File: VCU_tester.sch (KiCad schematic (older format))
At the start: 40 parts, among them J1 Conn_01x04_Male, J12 Conn_01x08_Male, J13 Conn_01x08_Male, J14 USB_C_Receptacle, J15 USB_B_Micro, J2 Screw_Terminal_01x02, J500 Conn_01x08_Female, J501 Conn_01x08_Female, J502 Conn_01x08_Female, J504 Conn_02x18_Odd_Even, J505 Conn_01x10_Female, J506 Conn_01x08_Female, J507 Conn_01x08_Female, J7 Conn_01x04_Male, P8 BeagleBone_Black_Header, P9 BeagleBone_Black_Header, U1 REF3020, U6 DS3231MZ, U7 DS3231MZ

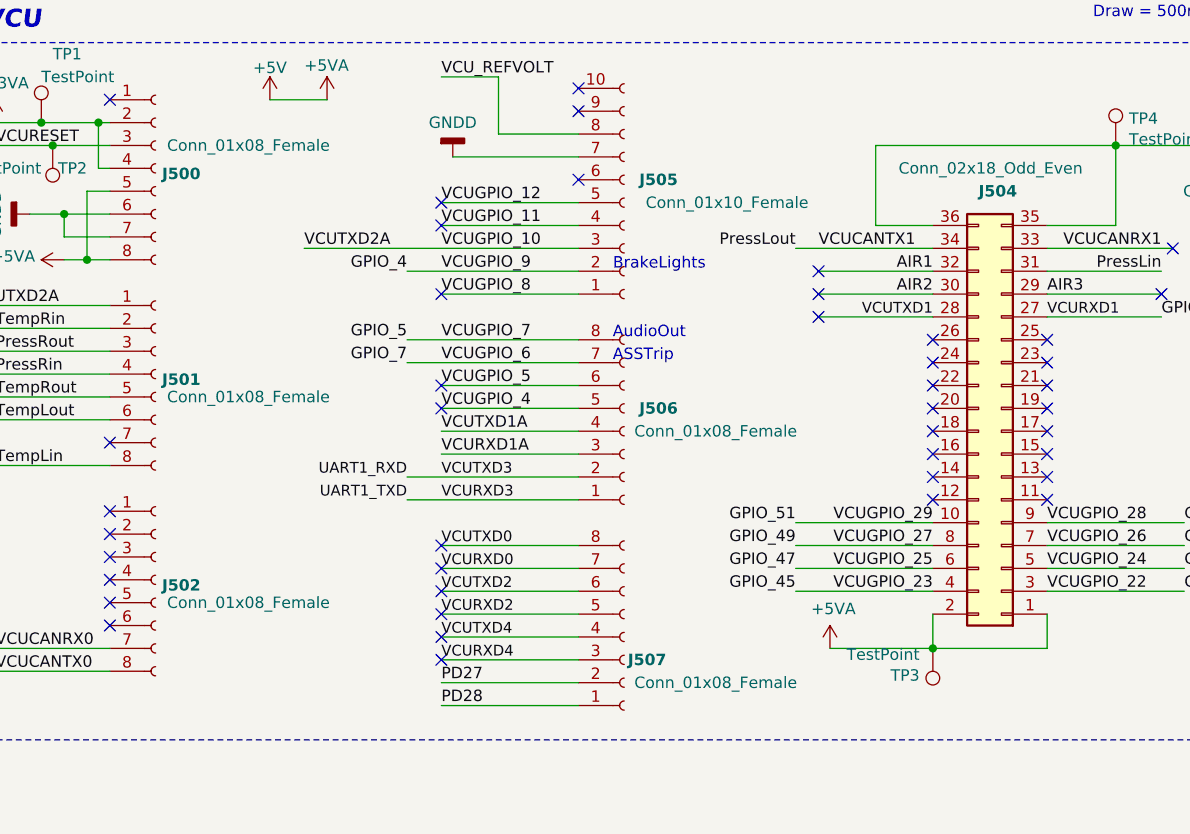
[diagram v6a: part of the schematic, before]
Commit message: placed vcu and beaglebone
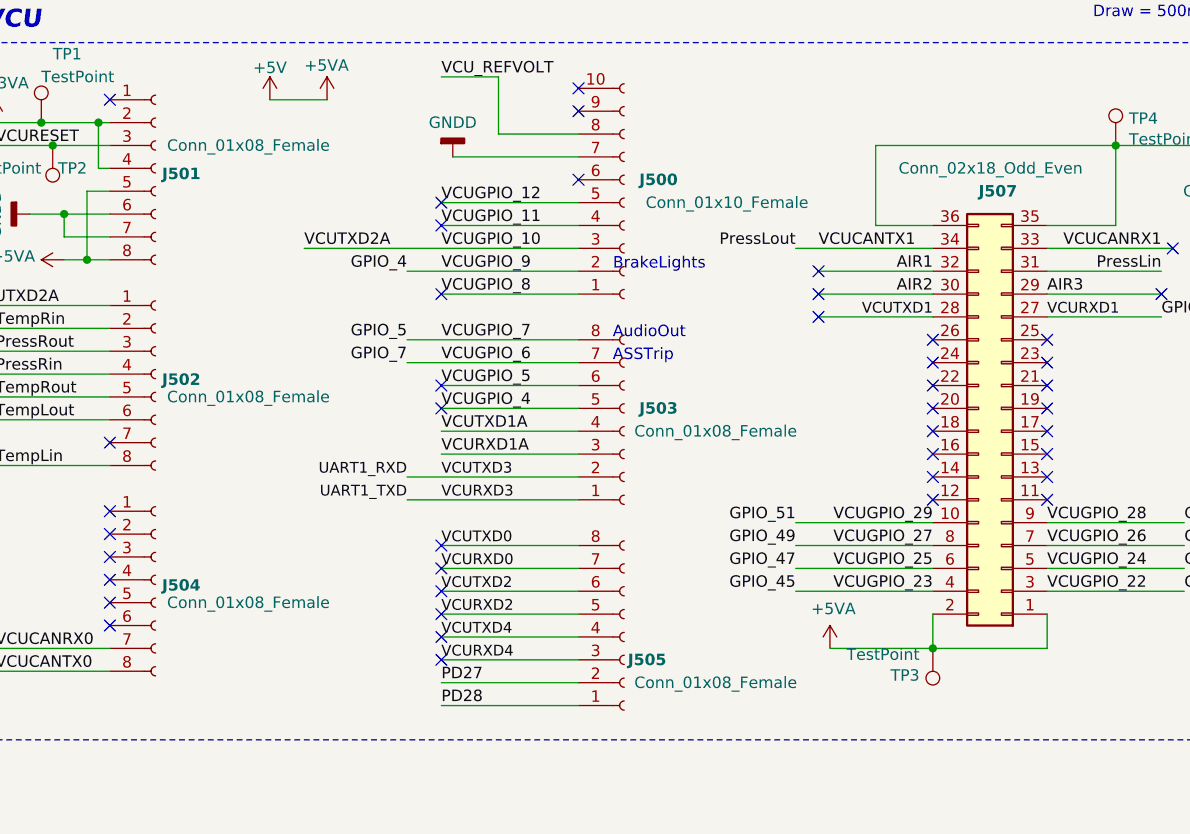
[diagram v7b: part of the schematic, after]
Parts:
- P8, P9: footprint Socket_BeagleBone_Black:Socket_BeagleBone_Black -> project:PinHeader_2x23_P2.54mm_Vertical_Flip
- renumbered J505 to J500, J500 to J501, J501 to J502, J506 to J503, J502 to J504, J507 to J505, J504 to J507
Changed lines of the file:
@@
 F 0 "P9" H 2400 3650 50  0000 C CNN
 F 1 "BeagleBone_Black_Header" V 2450 2500 50  0000 C CNN
-F 2 "Socket_BeagleBone_Black:Socket_BeagleBone_Black" H 2400 1600 60  0001 C CNN
+F 2 "project:PinHeader_2x23_P2.54mm_Vertical_Flip" H 2400 1600 60  0001 C CNN
 F 3 "" H 2400 1600 60  0000 C CNN
 F 4 "1528-1365-ND" H 2400 2450 50  0001 C CNN "Part"
@@
 F 0 "P8" H 4700 3650 50  0000 C CNN
 F 1 "BeagleBone_Black_Header" V 4750 2500 50  0000 C CNN
-F 2 "Socket_BeagleBone_Black:Socket_BeagleBone_Black" H 4700 1600 60  0001 C CNN
+F 2 "project:PinHeader_2x23_P2.54mm_Vertical_Flip" H 4700 1600 60  0001 C CNN
 F 3 "" H 4700 1600 60  0000 C CNN
 F 4 "1528-1365-ND" H 4700 2450 50  0001 C CNN "Part"
@@
 	2850 1200 2850 1150
 $Comp
-L Connector:Conn_01x08_Female J500
+L Connector:Conn_01x08_Female J501
 U 1 1 5E5FE8D2
 P 1750 6950
-F 0 "J500" H 1778 6926 50  0000 L CNB
+F 0 "J501" H 1778 6926 50  0000 L CNB
 F 1 "Conn_01x08_Female" H 1800 7050 50  0000 L CNN
 F 2 "Connector_PinSocket_2.54mm:PinSocket_1x08_P2.54mm_Vertical" H 1750 6950 50  0001 C CNN
@@
 $EndComp
 $Comp
-L Connector:Conn_01x08_Female J501
+L Connector:Conn_01x08_Female J502
 U 1 1 5E6082CD
 P 1750 7850
-F 0 "J501" H 1778 7826 50  0000 L CNB
+F 0 "J502" H 1778 7826 50  0000 L CNB
 F 1 "Conn_01x08_Female" H 1800 7750 50  0000 L CNN
 F 2 "Connector_PinSocket_2.54mm:PinSocket_1x08_P2.54mm_Vertical" H 1750 7850 50  0001 C CNN
@@
 $EndComp
 $Comp
-L Connector:Conn_01x08_Female J502
+L Connector:Conn_01x08_Female J504
 U 1 1 5E60D4FC
 P 1750 8750
-F 0 "J502" H 1778 8726 50  0000 L CNB
+F 0 "J504" H 1778 8726 50  0000 L CNB
 F 1 "Conn_01x08_Female" H 1800 8650 50  0000 L CNN
 F 2 "Connector_PinSocket_2.54mm:PinSocket_1x08_P2.54mm_Vertical" H 1750 8750 50  0001 C CNN
@@
 $EndComp
 $Comp
-L Connector_Generic:Conn_02x18_Odd_Even J504
+L Connector_Generic:Conn_02x18_Odd_Even J507
 U 1 1 5E625E8F
 P 5450 8100
-F 0 "J504" H 5550 7050 50  0000 R CNB
+F 0 "J507" H 5550 7050 50  0000 R CNB
 F 1 "Conn_02x18_Odd_Even" H 5900 6950 50  0000 R CNN
 F 2 "Connector_PinSocket_2.54mm:PinSocket_2x18_P2.54mm_Vertical" H 5450 8100 50  0001 C CNN
@@
 $EndComp
 $Comp
-L Connector:Conn_01x10_Female J505
+L Connector:Conn_01x10_Female J500
 U 1 1 5E6A0220
 P 3800 7100
-F 0 "J505" H 3950 7000 50  0000 C CNB
+F 0 "J500" H 3950 7000 50  0000 C CNB
 F 1 "Conn_01x10_Female" H 4250 7100 50  0000 C CNN
 F 2 "Connector_PinSocket_2.54mm:PinSocket_1x10_P2.54mm_Vertical" H 3800 7100 50  0001 C CNN
@@
 $EndComp
 $Comp
-L Connector:Conn_01x08_Female J507
+L Connector:Conn_01x08_Female J505
 U 1 1 5E6A022C
 P 3800 9000
-F 0 "J507" H 3900 9100 50  0000 C CNB
+F 0 "J505" H 3900 9100 50  0000 C CNB
 F 1 "Conn_01x08_Female" H 4200 9200 50  0000 C CNN
 F 2 "Connector_PinSocket_2.54mm:PinSocket_1x08_P2.54mm_Vertical" H 3800 9000 50  0001 C CNN
@@
 $EndComp
 $Comp
-L Connector:Conn_01x08_Female J506
+L Connector:Conn_01x08_Female J503
 U 1 1 5E6A0226
 P 3800 8100
-F 0 "J506" H 3950 8000 50  0000 C CNB
+F 0 "J503" H 3950 8000 50  0000 C CNB
 F 1 "Conn_01x08_Female" H 4200 8100 50  0000 C CNN
 F 2 "Connector_PinSocket_2.54mm:PinSocket_1x08_P2.54mm_Vertical" H 3800 8100 50  0001 C CNN

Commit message: new, compact (and sexy) design
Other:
- moved on the sheet: BT1, U1
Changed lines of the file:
@@
 RTC VCU
 Wire Wire Line
-	10750 8450 11400 8450
-Text Label 10750 8450 0    50   ~ 0
+	9950 8450 10600 8450
+Text Label 9950 8450 0    50   ~ 0
 VCU_REFVOLT
 $Comp
 L Reference_Voltage:REF3020 U1
 U 1 1 5F9A6E14
-P 11700 8450
-F 0 "U1" H 11470 8496 50  0000 R CNN
-F 1 "REF3020" H 11470 8405 50  0000 R CIN
-F 2 "Package_TO_SOT_SMD:SOT-23" H 11700 8000 50  0001 C CIN
-F 3 "http://www.ti.com/lit/ds/symlink/ref3033.pdf" H 11800 8100 50  0001 C CIN
-F 4 "296-26321-1-ND" H 11700 8450 50  0001 C CNN "Part"
-	1    11700 8450
+P 10900 8450
+F 0 "U1" H 10670 8496 50  0000 R CNN
+F 1 "REF3020" H 10670 8405 50  0000 R CIN
+F 2 "Package_TO_SOT_SMD:SOT-23" H 10900 8000 50  0001 C CIN
+F 3 "http://www.ti.com/lit/ds/symlink/ref3033.pdf" H 11000 8100 50  0001 C CIN
+F 4 "296-26321-1-ND" H 10900 8450 50  0001 C CNN "Part"
+	1    10900 8450
 	-1   0    0    -1
 $EndComp
@@
 L power:GNDD #PWR0104
 U 1 1 5F9A8026
-P 11800 8750
-F 0 "#PWR0104" H 11800 8500 50  0001 C CNN
-F 1 "GNDD" H 11804 8595 50  0000 C CNN
-F 2 "" H 11800 8750 50  0001 C CNN
-F 3 "" H 11800 8750 50  0001 C CNN
-	1    11800 8750
+P 11000 8750
+F 0 "#PWR0104" H 11000 8500 50  0001 C CNN
+F 1 "GNDD" H 11004 8595 50  0000 C CNN
+F 2 "" H 11000 8750 50  0001 C CNN
+F 3 "" H 11000 8750 50  0001 C CNN
+	1    11000 8750
 	1    0    0    -1
 $EndComp
@@
 L power:+5V #PWR0105
 U 1 1 5F9AA125
-P 11800 8150
-F 0 "#PWR0105" H 11800 8000 50  0001 C CNN
-F 1 "+5V" H 11800 8290 50  0000 C CNN
-F 2 "" H 11800 8150 60  0000 C CNN
-F 3 "" H 11800 8150 60  0000 C CNN
-	1    11800 8150
-	1    0    0    -1
-$EndComp
-Text Notes 11000 7950 0    50   ~ 0
+P 11000 8150
+F 0 "#PWR0105" H 11000 8000 50  0001 C CNN
+F 1 "+5V" H 11000 8290 50  0000 C CNN
+F 2 "" H 11000 8150 60  0000 C CNN
+F 3 "" H 11000 8150 60  0000 C CNN
+	1    11000 8150
+	1    0    0    -1
+$EndComp
+Text Notes 10200 7950 0    50   ~ 0
 VCU Reference Voltage\n2.048V
 $Comp
@@
 L Device:Battery_Cell BT1
 U 1 1 601EDE3A
-P 10450 4550
-F 0 "BT1" H 10568 4646 50  0000 L CNN
-F 1 "Battery_Cell" H 10568 4555 50  0000 L CNN
-F 2 "Battery:BatteryHolder_MPD_BC2003_1x2032" V 10450 4610 50  0001 C CNN
-F 3 "~" V 10450 4610 50  0001 C CNN
-F 4 "BU2032SM-FH-GCT-ND" H 10450 4550 50  0001 C CNN "Part"
-	1    10450 4550
+P 10800 4550
+F 0 "BT1" H 10918 4646 50  0000 L CNN
+F 1 "Battery_Cell" H 10918 4555 50  0000 L CNN
+F 2 "Battery:BatteryHolder_MPD_BC2003_1x2032" V 10800 4610 50  0001 C CNN
+F 3 "~" V 10800 4610 50  0001 C CNN
+F 4 "BU2032SM-FH-GCT-ND" H 10800 4550 50  0001 C CNN "Part"
+	1    10800 4550
 	1    0    0    -1
 $EndComp
@@
 L power:GNDD #PWR018
 U 1 1 602101F4
-P 10450 4650
-F 0 "#PWR018" H 10450 4400 50  0001 C CNN
-F 1 "GNDD" H 10450 4500 50  0000 C CNN
-F 2 "" H 10450 4650 60  0000 C CNN
-F 3 "" H 10450 4650 60  0000 C CNN
-	1    10450 4650
-	1    0    0    -1
-$EndComp
-Wire Wire Line
-	10450 4350 10450 4300
-Wire Wire Line
-	10450 4300 10200 4300
-Text Label 10200 4300 0    50   ~ 0
+P 10800 4650
+F 0 "#PWR018" H 10800 4400 50  0001 C CNN
+F 1 "GNDD" H 10800 4500 50  0000 C CNN
+F 2 "" H 10800 4650 60  0000 C CNN
+F 3 "" H 10800 4650 60  0000 C CNN
+	1    10800 4650
+	1    0    0    -1
+$EndComp
+Wire Wire Line
+	10800 4350 10800 4300
+Wire Wire Line
+	10800 4300 10550 4300
+Text Label 10550 4300 0    50   ~ 0
 RTC_VBAT
 Text Label 7950 3600 1    50   ~ 0
@@
 L power:PWR_FLAG #FLG0108
 U 1 1 6081FF4F
-P 10200 4300
-F 0 "#FLG0108" H 10200 4375 50  0001 C CNN
-F 1 "PWR_FLAG" V 10200 4427 50  0000 L CNN
-F 2 "" H 10200 4300 50  0001 C CNN
-F 3 "~" H 10200 4300 50  0001 C CNN
-	1    10200 4300
+P 10550 4300
+F 0 "#FLG0108" H 10550 4375 50  0001 C CNN
+F 1 "PWR_FLAG" V 10550 4427 50  0000 L CNN
+F 2 "" H 10550 4300 50  0001 C CNN
+F 3 "~" H 10550 4300 50  0001 C CNN
+	1    10550 4300
 	0    -1   -1   0
 $EndComp
